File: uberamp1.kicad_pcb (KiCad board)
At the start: 2 copper layers, 152.1 x 125.2 mm, 238 parts, among them IC1 TPA3255, IC2 TPA3255, J1 Conn_01x04, J2 Conn_01x04, U1 Opamp_Dual, U2 Opamp_Dual, U3 Opamp_Dual, U4 Opamp_Dual, U5 Opamp_Dual, U6 Opamp_Dual, U7 Opamp_Dual, U8 Opamp_Dual

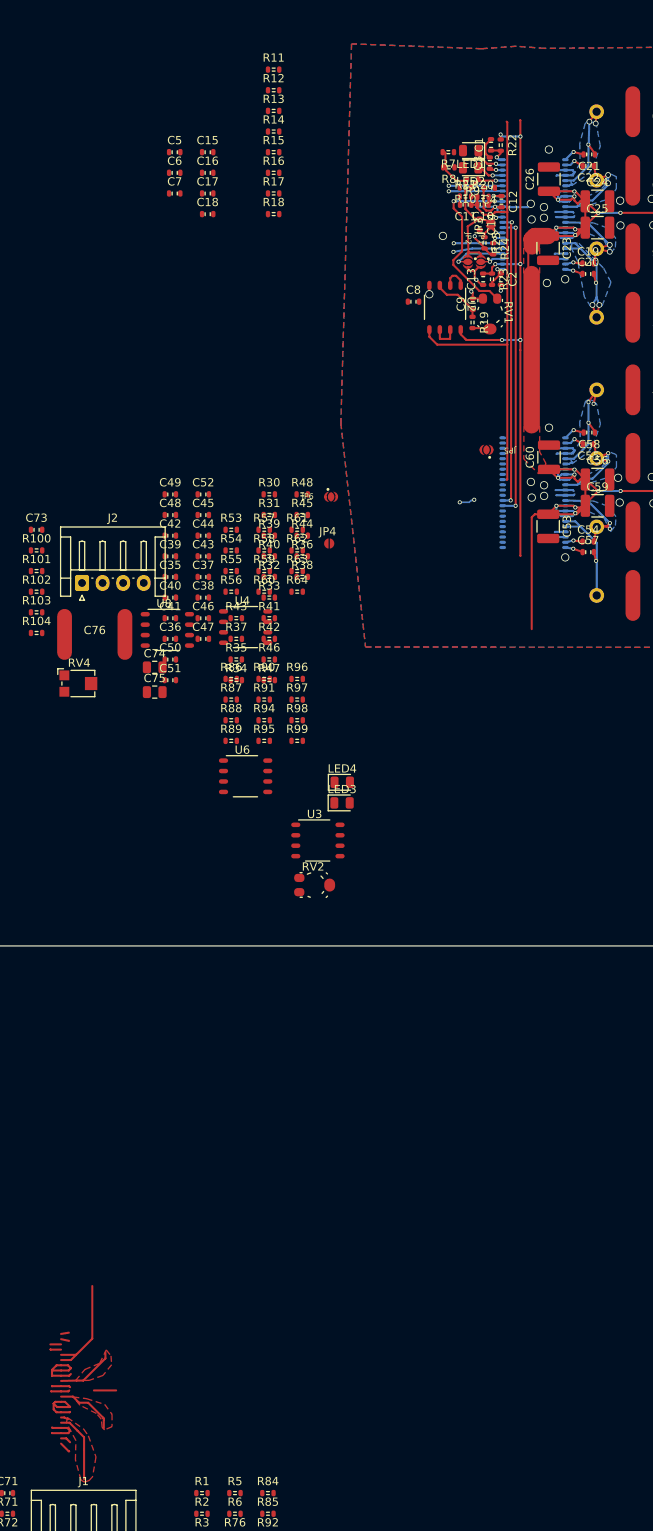
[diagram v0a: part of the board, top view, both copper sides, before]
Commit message: add bypass caps to opamps + swap poweramps + layout progress
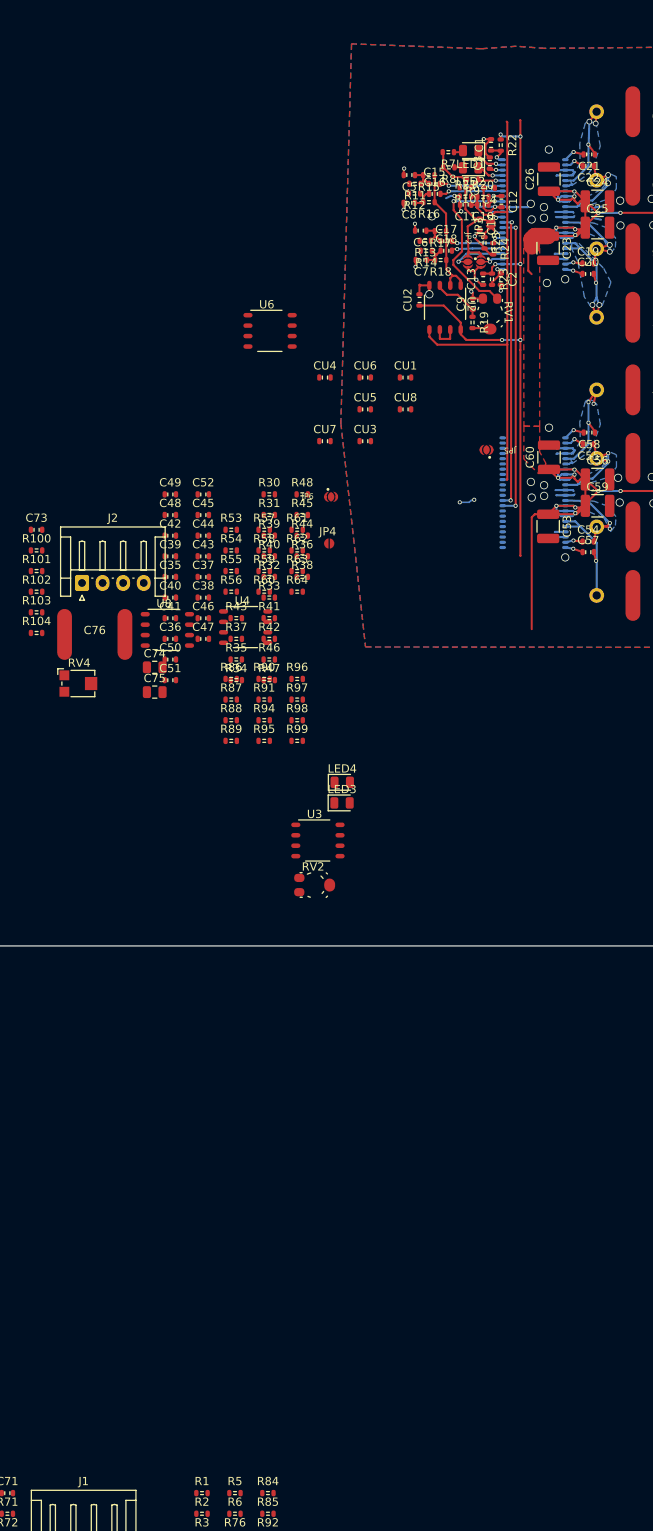
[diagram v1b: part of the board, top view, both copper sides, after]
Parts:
- added CU1: 10u, invendelirium_audio:C_0603, F.Cu at (84.5, 74.3)
- added CU2: 10u, invendelirium_audio:C_0603, F.Cu at (86.2, 64.9)
- added CU3: 10u, invendelirium_audio:C_0603, F.Cu at (79.6, 82.1)
- added CU4: 10u, invendelirium_audio:C_0603, F.Cu at (74.7, 74.3)
- added CU5: 10u, invendelirium_audio:C_0603, F.Cu at (79.6, 78.2)
- added CU6: 10u, invendelirium_audio:C_0603, F.Cu at (79.6, 74.3)
- added CU7: 10u, invendelirium_audio:C_0603, F.Cu at (74.7, 82.1)
- added CU8: 10u, invendelirium_audio:C_0603, F.Cu at (84.5, 78.2)
- C14, C43: value 10u -> 1uF
- moved U6 54.2 mm to (68.0, 68.7)
- moved C7 31.1 mm to (86.4, 60.0), turned to 180 degrees
- moved C6 30.7 mm to (86.3, 56.5), turned to 180 degrees
- moved C17 29.6 mm to (89.4, 57.7)
- moved C18 29.4 mm to (89.4, 58.9)
- moved C5 28.7 mm to (84.9, 49.7), turned to 180 degrees
- moved C15 27.8 mm to (88.0, 50.8)
- moved C16 27.7 mm to (88.0, 52.0)
- moved R13 24.3 mm to (86.9, 57.7), turned to 180 degrees
- moved R14 23.6 mm to (87.0, 58.9), turned to 180 degrees
- moved R11 22.1 mm to (85.6, 50.8), turned to 180 degrees
- moved R12 21.2 mm to (85.6, 52.0), turned to 180 degrees
- moved R18 21.1 mm to (88.7, 60.0), turned to 180 degrees
- moved R17 20.8 mm to (88.7, 56.5), turned to 180 degrees
- moved R16 19.2 mm to (87.3, 53.0), turned to 180 degrees
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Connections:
- R2 pad 2: /poweramp1/in0 -> /poweramp/in0
- R6 pad 2: /poweramp1/in1 -> /poweramp/in1
- R63 pad 2: /poweramp1/in3 -> /poweramp/in3
- R64 pad 2: /poweramp1/in2 -> /poweramp/in2
- R82 pad 2: /poweramp/in1 -> /poweramp1/in1
- R83 pad 2: /poweramp/in0 -> /poweramp1/in0
- R98 pad 2: /poweramp/in3 -> /poweramp1/in3
- R99 pad 2: /poweramp/in2 -> /poweramp1/in2
- U1 pad 1: /poweramp1/in1 -> /poweramp/in1
- U1 pad 7: /poweramp1/in0 -> /poweramp/in0
- U2 pad 6: /poweramp/input_ref -> /inputref
- U2 pad 7: /poweramp/input_ref -> /inputref
- U3 pad 6: /inputref -> /poweramp1/input_ref
- U3 pad 7: /inputref -> /poweramp1/input_ref
- U4 pad 1: /poweramp1/in3 -> /poweramp/in3
- U4 pad 7: /poweramp1/in2 -> /poweramp/in2
- U5 pad 1: /poweramp/in1 -> /poweramp1/in1
- U5 pad 7: /poweramp/in0 -> /poweramp1/in0
- U6 pad 1: /poweramp/in3 -> /poweramp1/in3
- U6 pad 7: /poweramp/in2 -> /poweramp1/in2
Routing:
- net PVDD: track 296.5 -> 240.8 mm
- net /poweramp/trim: track 3.11 -> 16.3 mm
- net /poweramp1/sw1: track 19.7 -> 12.2 mm
- net /poweramp1/sw2: track 19.7 -> 12.5 mm
- net /12V: track 69.6 -> 76.3 mm
- net /poweramp/input_ref: track 3.49 -> 0.00 mm
- net /inputref: track 0.00 -> 3.49 mm
- net Net-(C17-Pad1): track 0.00 -> 3.33 mm
- net Net-(C18-Pad1): track 0.00 -> 3.17 mm
- net Net-(C16-Pad1): track 0.00 -> 3.13 mm
- net Net-(C15-Pad1): track 0.00 -> 3.03 mm
- net Net-(IC2-23_BST_D): track 4.03 -> 2.64 mm
- net Net-(IC2-24_BST_C): track 3.77 -> 2.47 mm
- net Net-(LED1-A): track 0.00 -> 1.17 mm
- net /poweramp/in_d: track 6.55 -> 7.70 mm
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- removed copper zone on F.Cu, net /poweramp1/sw0
- removed copper zone on F.Cu, net /poweramp1/sw1
- removed copper zone on F.Cu, net /poweramp1/sw2

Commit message: route 1 preamp
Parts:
- added s0: sum0, TestPoint:TestPoint_Pad_D1.5mm, B.Cu at (81.8, 47.1)
- added s1: sum0, TestPoint:TestPoint_Pad_D1.5mm, B.Cu at (81.8, 43.8)
- added s2: sum0, TestPoint:TestPoint_Pad_D1.5mm, F.Cu at (59.0, 94.2)
- added s3: sum0, TestPoint:TestPoint_Pad_D1.5mm, F.Cu at (59.0, 97.8)
- added s4: sum0, TestPoint:TestPoint_Pad_D1.5mm, F.Cu at (46.4, 63.1)
- added s5: sum0, TestPoint:TestPoint_Pad_D1.5mm, F.Cu at (46.4, 66.7)
- added s6: sum0, TestPoint:TestPoint_Pad_D1.5mm, F.Cu at (62.9, 123.4)
- added s7: sum0, TestPoint:TestPoint_Pad_D1.5mm, F.Cu at (62.9, 127.0)
- moved R78 182.4 mm to (80.9, 54.1), turned to 180 degrees
- moved U5 179.3 mm to (80.2, 61.7), turned to -90 degrees
- moved R80 178.7 mm to (80.9, 39.7), turned to 180 degrees
- moved R93 177.2 mm to (80.9, 40.9), turned to 180 degrees
- moved U1 176.7 mm to (80.1, 46.1), turned to -90 degrees
- moved R76 176.0 mm to (78.7, 39.7)
- moved R92 174.5 mm to (78.7, 40.9)
- moved R2 171.8 mm to (80.9, 42.0)
- moved R65 169.2 mm to (52.2, 59.1)
- moved R66 169.2 mm to (52.2, 61.6)
- moved R67 169.2 mm to (52.2, 64.1)
- moved R68 169.2 mm to (52.2, 66.7)
- moved R69 169.2 mm to (56.2, 59.1)
- moved R70 169.2 mm to (56.2, 61.6)
- moved R77 169.2 mm to (56.2, 64.1)
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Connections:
- net /feedbass_preamp/out renamed /fb0
- net /feedbass_preamp/~out renamed /~fb0
- net /feedbass_preamp1/out renamed /fb1
- net /feedbass_preamp1/~out renamed /~fb1
- R1 pad 2: Net-(U1B--) -> Net-(U1A--)
- R2 pad 1: Net-(U1B--) -> Net-(U1A--)
- R3 pad 2: Net-(U1A--) -> Net-(U1B--)
- R4 pad 2: Net-(U1A--) -> Net-(U1B--)
- R5 pad 2: Net-(U1A--) -> Net-(U1B--)
- R53 pad 2: Net-(U4A--) -> Net-(U4B--)
- R54 pad 2: Net-(U4A--) -> Net-(U4B--)
- R55 pad 2: Net-(U4A--) -> Net-(U4B--)
- R56 pad 2: Net-(U4A--) -> Net-(U4B--)
- R57 pad 2: Net-(U4A--) -> Net-(U4B--)
- R58 pad 2: Net-(U4B--) -> Net-(U4A--)
- R59 pad 2: Net-(U4B--) -> Net-(U4A--)
- R6 pad 1: Net-(U1A--) -> Net-(U1B--)
- R60 pad 2: Net-(U4B--) -> Net-(U4A--)
- R61 pad 2: Net-(U4B--) -> Net-(U4A--)
- R62 pad 2: Net-(U4B--) -> Net-(U4A--)
- R63 pad 1: Net-(U4A--) -> Net-(U4B--)
- R64 pad 1: Net-(U4B--) -> Net-(U4A--)
- R65 pad 2: Net-(U5A--) -> Net-(U5B--)
- R66 pad 2: Net-(U5A--) -> Net-(U5B--)
- R67 pad 2: Net-(U5A--) -> Net-(U5B--)
- R68 pad 2: Net-(U5A--) -> Net-(U5B--)
- R69 pad 2: Net-(U5A--) -> Net-(U5B--)
- R70 pad 2: Net-(U5B--) -> Net-(U5A--)
- R76 pad 2: Net-(U1B--) -> Net-(U1A--)
- R77 pad 2: Net-(U5B--) -> Net-(U5A--)
- R78 pad 2: Net-(U5B--) -> Net-(U5A--)
- R79 pad 2: Net-(U5B--) -> Net-(U5A--)
- R80 pad 2: Net-(U1B--) -> Net-(U1A--)
- R81 pad 2: Net-(U5B--) -> Net-(U5A--)
- R82 pad 1: Net-(U5A--) -> Net-(U5B--)
- R83 pad 1: Net-(U5B--) -> Net-(U5A--)
- R84 pad 2: Net-(U1A--) -> Net-(U1B--)
- R85 pad 2: Net-(U1A--) -> Net-(U1B--)
- R86 pad 2: Net-(U6A--) -> Net-(U6B--)
- R87 pad 2: Net-(U6A--) -> Net-(U6B--)
- R88 pad 2: Net-(U6A--) -> Net-(U6B--)
- R89 pad 2: Net-(U6A--) -> Net-(U6B--)
- R90 pad 2: Net-(U6A--) -> Net-(U6B--)
- R91 pad 2: Net-(U6B--) -> Net-(U6A--)
- R92 pad 2: Net-(U1B--) -> Net-(U1A--)
- R93 pad 2: Net-(U1B--) -> Net-(U1A--)
- R94 pad 2: Net-(U6B--) -> Net-(U6A--)
- R95 pad 2: Net-(U6B--) -> Net-(U6A--)
- R96 pad 2: Net-(U6B--) -> Net-(U6A--)
- R97 pad 2: Net-(U6B--) -> Net-(U6A--)
- R98 pad 1: Net-(U6A--) -> Net-(U6B--)
- R99 pad 1: Net-(U6B--) -> Net-(U6A--)
- U1 pad 1: /poweramp/in1 -> /poweramp/in0
- U1 pad 7: /poweramp/in0 -> /poweramp/in1
- U4 pad 1: /poweramp/in3 -> /poweramp/in2
- U4 pad 7: /poweramp/in2 -> /poweramp/in3
- U5 pad 1: /poweramp1/in1 -> /poweramp1/in0
- U5 pad 7: /poweramp1/in0 -> /poweramp1/in1
- U6 pad 1: /poweramp1/in3 -> /poweramp1/in2
- U6 pad 7: /poweramp1/in2 -> /poweramp1/in3
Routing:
- net /12V: track 76.3 -> 198.2 mm, vias 6 -> 14
- net /inputref: track 3.49 -> 100.0 mm, vias 0 -> 2
- net /~fb1: track 0.00 -> 92.6 mm, vias 0 -> 4
- net /~fb0: track 0.00 -> 91.3 mm, vias 0 -> 4
- net /fb1: track 0.00 -> 88.3 mm, vias 0 -> 4
- net /fb0: track 0.00 -> 86.0 mm, vias 0 -> 4
- net /poweramp/input_ref_z: track 61.4 -> 106.2 mm
- net GND: track 66.0 -> 110.3 mm, vias 45 -> 61
- net /poweramp1/AVDD: track 0.00 -> 23.4 mm, vias 0 -> 2
- net /poweramp1/DVDD: track 0.00 -> 21.6 mm, vias 0 -> 1
- net /poweramp1/trim: track 0.00 -> 16.3 mm
- net PVDD: track 240.8 -> 225.0 mm
- net Net-(U1B--): track 0.00 -> 10.9 mm, vias 0 -> 1
- net Net-(U1A--): track 0.00 -> 10.9 mm, vias 0 -> 1
- net /poweramp1/in_d: track 0.00 -> 7.70 mm, vias 0 -> 1
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- added copper zone on B.Cu, net /poweramp1/sw3

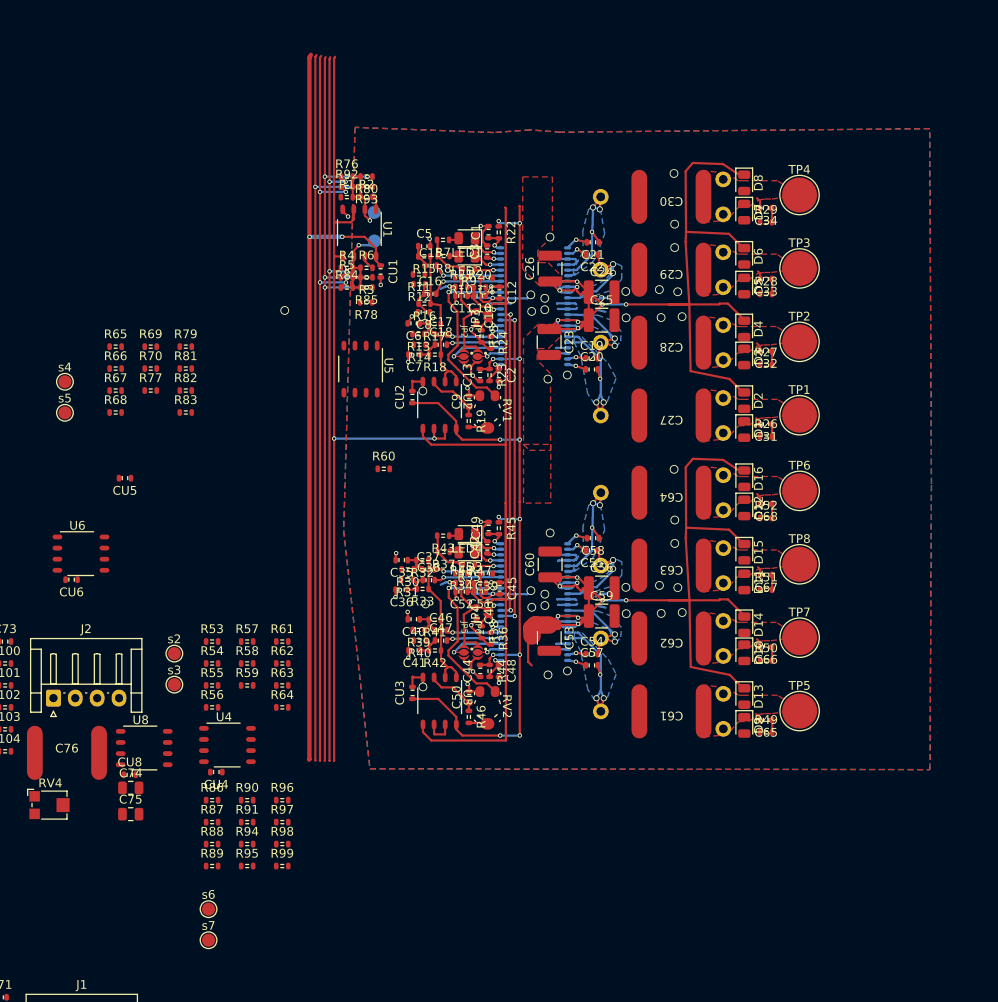
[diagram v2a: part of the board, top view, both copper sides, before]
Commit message: route all preamps
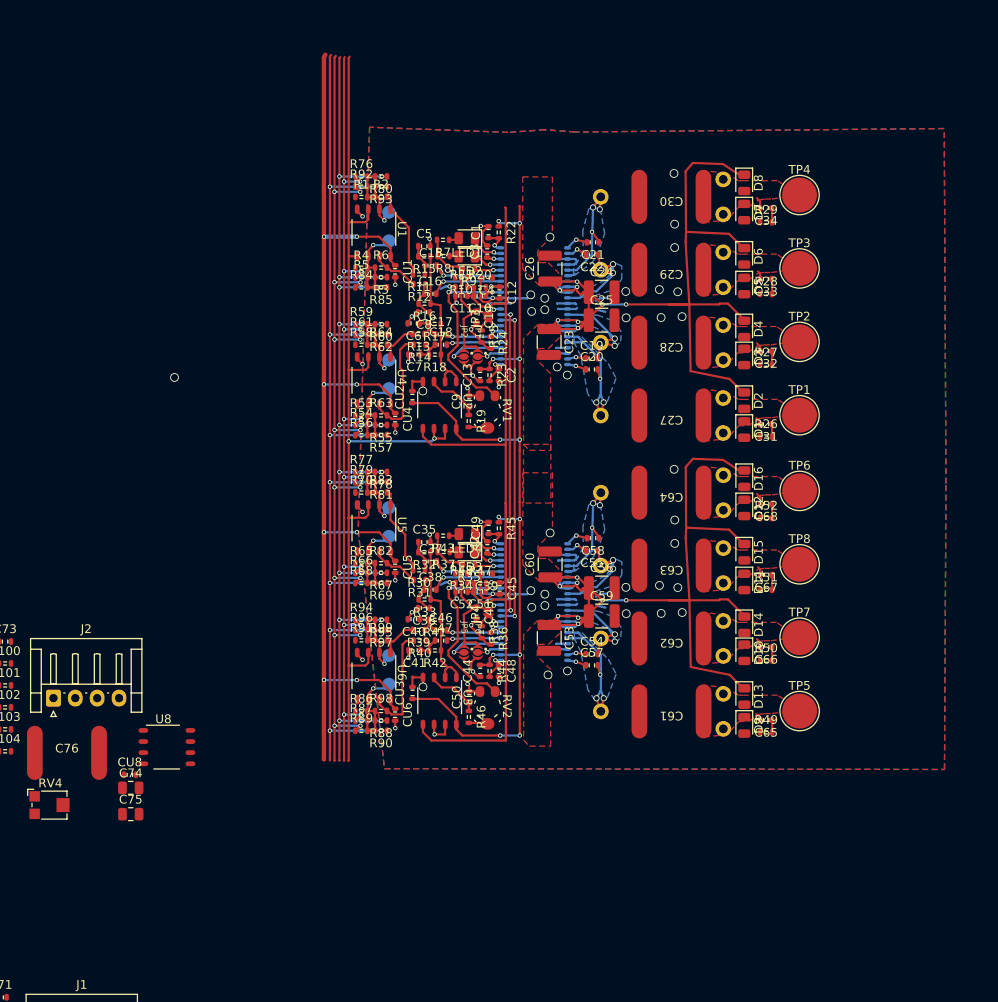
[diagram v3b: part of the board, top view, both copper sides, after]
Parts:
- s2, s3, s4, s5, s6, s7: moved to B.Cu
- moved CU4 45.2 mm to (84.2, 67.4), turned to -90 degrees
- moved U4 44.9 mm to (81.8, 63.0), turned to -90 degrees
- moved s3 44.5 mm to (83.5, 60.6), turned to 180 degrees
- moved R59 43.3 mm to (80.3, 56.6)
- moved R64 43.0 mm to (82.6, 58.9)
- moved s4 41.1 mm to (83.5, 80.8), turned to 180 degrees
- moved CU6 40.1 mm to (84.2, 101.2), turned to -90 degrees
- moved R62 39.3 mm to (82.6, 57.7), turned to 180 degrees
- moved s2 39.0 mm to (83.5, 63.9), turned to 180 degrees
- moved R58 38.7 mm to (80.3, 58.9)
- moved s5 38.6 mm to (83.5, 77.5), turned to 180 degrees
- moved s7 38.5 mm to (83.5, 94.4), turned to 180 degrees
- moved R69 37.7 mm to (82.6, 86.1), turned to 180 degrees
- moved R65 37.5 mm to (80.3, 83.9)
- moved R67 36.8 mm to (82.6, 85.0), turned to 180 degrees
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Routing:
- net /~fb1: track 92.6 -> 131.6 mm, vias 4 -> 16
- net /~fb0: track 91.3 -> 123.8 mm, vias 4 -> 16
- net /12V: track 198.2 -> 229.3 mm, vias 14 -> 20
- net /fb1: track 88.3 -> 111.3 mm, vias 4 -> 16
- net /fb0: track 86.0 -> 102.7 mm, vias 4 -> 16
- net /poweramp/in3: track 0.00 -> 13.4 mm
- net /poweramp1/in3: track 0.00 -> 13.0 mm
- net Net-(U6B--): track 0.00 -> 10.9 mm, vias 0 -> 1
- net Net-(U5B--): track 0.00 -> 10.9 mm, vias 0 -> 1
- net Net-(U4B--): track 0.00 -> 10.9 mm, vias 0 -> 1
- net Net-(U6A--): track 0.00 -> 10.9 mm, vias 0 -> 1
- net Net-(U4A--): track 0.00 -> 10.9 mm, vias 0 -> 1
- net Net-(U5A--): track 0.00 -> 10.9 mm, vias 0 -> 1
- net /poweramp1/in0: track 0.00 -> 10.3 mm
- net /inputref: track 100.0 -> 109.1 mm
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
